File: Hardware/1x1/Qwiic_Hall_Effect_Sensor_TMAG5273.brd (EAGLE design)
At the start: 25.4 x 25.4 mm, 52 parts, among them J1 QWIIC_RIGHT_ANGLE, J2 QWIIC_RIGHT_ANGLE, Q1 20V/4.2A/52mΩ/1.4W, U1 TMAG5273

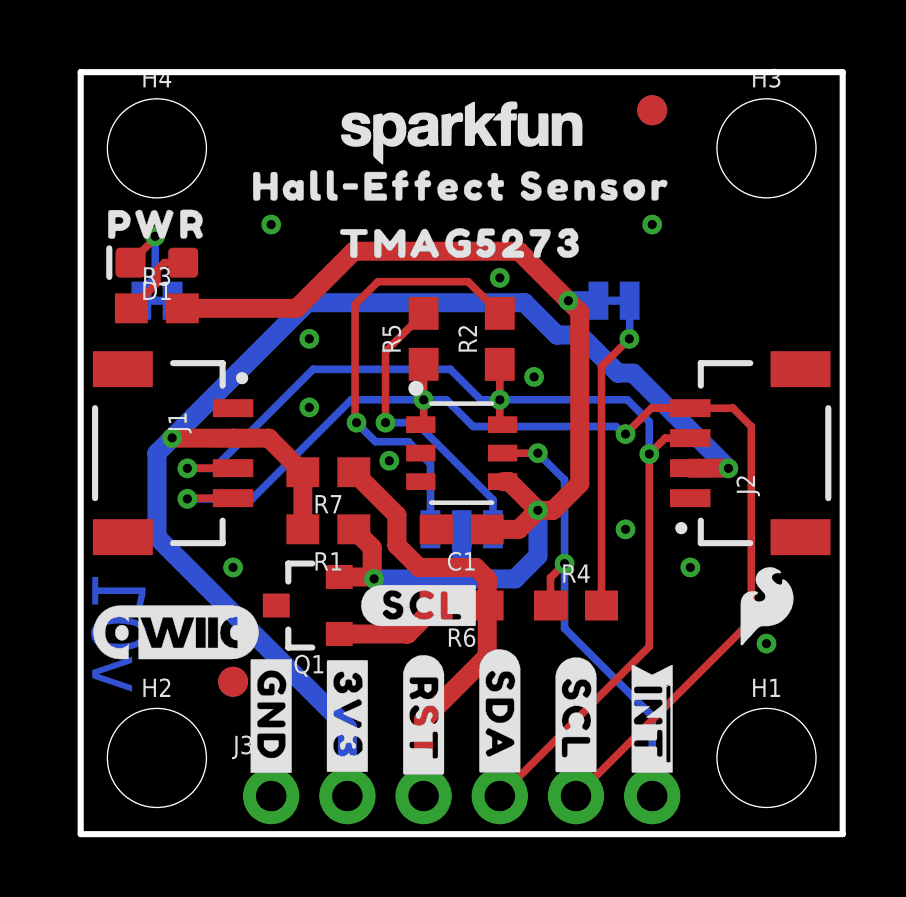
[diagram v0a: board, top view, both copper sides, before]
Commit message: Updates for design review
Changed LED and associated resistor to have the correct part and value; added dimension lines and further notes on the layout; adjusted aesthetics in schematic to now be the same as each other (minus the change in Qwiic connectors and number of standoffs)
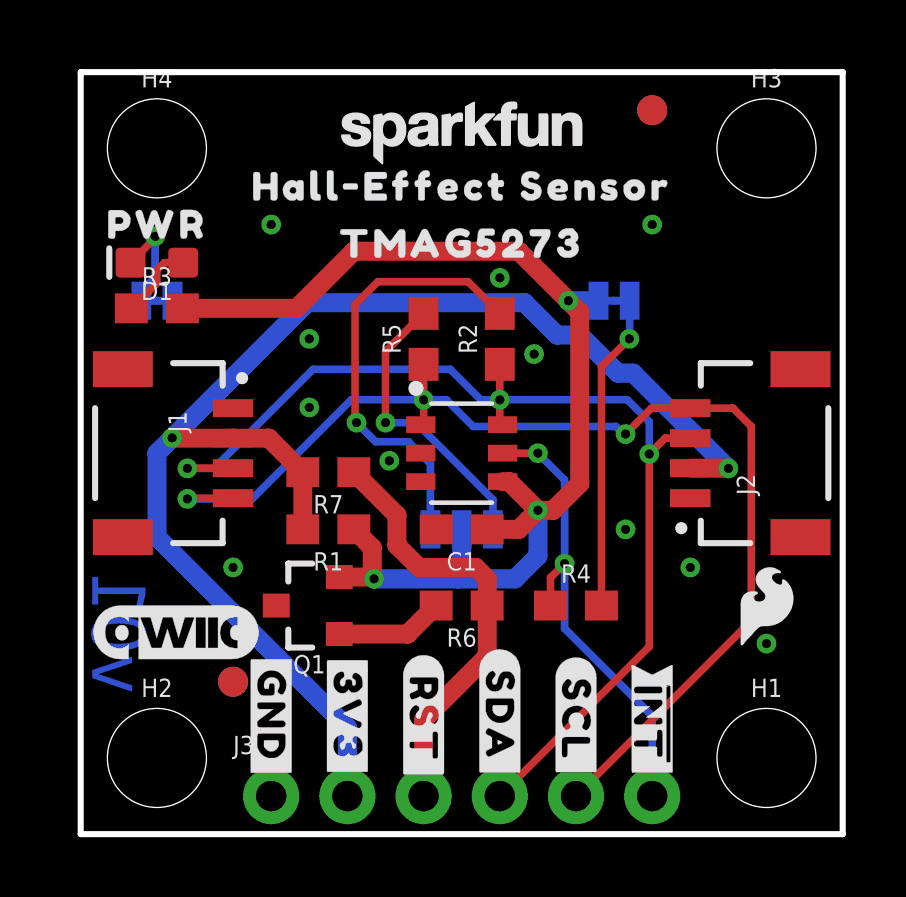
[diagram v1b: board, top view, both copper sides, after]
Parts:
- removed U$15: (no value), output:#SCL#5281
- D1: value RED -> Red
- R3: value 1k -> 4.7k
- moved FRAME1 16.6 mm to (-6.35, -40.6)
- moved LOGO5 16.5 mm to (44.5, 50.8)
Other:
- board text added: "Solder Mask: Red Thickness: 1.6mm Two layer design Finish: HASL Lead-Free Copper Weight: 1oz Material: TG135-140"
- board text added: "Units in inches"

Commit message: Ready for review
Updates from ENG Checklist - Small tweaks added  - updated ordering of PTH headers for SDA and SCL, fixed final errors on design
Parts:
- moved U$13 5.08 mm to (16.5, 4.70)
- moved U$5 5.08 mm to (16.5, 3.81)
- moved U$14 2.54 mm to (11.4, 3.94)
- moved U$16 2.54 mm to (14.0, 3.81)
- moved U$3 2.54 mm to (11.4, 3.94)
- moved U$4 2.54 mm to (14.0, 3.81)
- turned U$18 to 270 degrees
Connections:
- net GPIO: now also J3.5; no longer J3.3
- net SCL: now also J3.4; no longer J3.5
- net SDA: now also J3.3; no longer J3.4
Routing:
- net SCL: track 39.6 -> 42.1 mm
- net SDA: track 37.2 -> 39.7 mm
- net GPIO: track 14.6 -> 15.0 mm, vias 0 -> 1
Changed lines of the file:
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@@
 <layer number="37" name="tTest" color="7" fill="1" visible="no" active="yes"/>
 <layer number="38" name="bTest" color="7" fill="1" visible="no" active="yes"/>
-<layer number="39" name="tKeepout" color="4" fill="11" visible="yes" active="yes"/>
-<layer number="40" name="bKeepout" color="1" fill="11" visible="yes" active="yes"/>
-<layer number="41" name="tRestrict" color="4" fill="10" visible="yes" active="yes"/>
-<layer number="42" name="bRestrict" color="1" fill="10" visible="yes" active="yes"/>
+<layer number="39" name="tKeepout" color="4" fill="11" visible="no" active="yes"/>
+<layer number="40" name="bKeepout" color="1" fill="11" visible="no" active="yes"/>
+<layer number="41" name="tRestrict" color="4" fill="10" visible="no" active="yes"/>
+<layer number="42" name="bRestrict" color="1" fill="10" visible="no" active="yes"/>
 <layer number="43" name="vRestrict" color="2" fill="10" visible="no" active="yes"/>
 <layer number="44" name="Drills" color="7" fill="1" visible="no" active="yes"/>
@@
 <element name="U$2" library="output" package="#GND#36" value="" x="6.35" y="3.937" smashed="yes" rot="R270"/>
 <element name="U$1" library="output" package="#3V3#37" value="" x="8.89" y="3.937" smashed="yes" rot="R270"/>
-<element name="U$3" library="output" package="#SDA#37" value="" x="13.97" y="3.937" smashed="yes" rot="R270"/>
-<element name="U$4" library="output" package="#SCL#38" value="" x="16.51" y="3.81" smashed="yes" rot="R270"/>
+<element name="U$3" library="output" package="#SDA#37" value="" x="11.43" y="3.937" smashed="yes" rot="R270"/>
+<element name="U$4" library="output" package="#SCL#38" value="" x="13.97" y="3.81" smashed="yes" rot="R270"/>
 <element name="U$6" library="output" package="##INT#40" value="" x="19.05" y="3.683" smashed="yes" rot="R270"/>
 <element name="U$7" library="output" package="PWR41" value="" x="2.54" y="20.32" smashed="yes"/>
@@
 <attribute name="VALUE" x="7.62" y="9.271" size="0.6096" layer="27" font="vector" ratio="20" rot="R180" align="top-center"/>
 </element>
-<element name="U$13" library="output" package="#RESET#5278" value="" x="11.43" y="4.699" smashed="yes" rot="MR270"/>
-<element name="U$5" library="output" package="#RST#5279" value="" x="11.43" y="3.81" smashed="yes" rot="R270"/>
-<element name="U$14" library="output" package="#SDA#5280" value="" x="13.97" y="3.937" smashed="yes" rot="MR270"/>
-<element name="U$16" library="output" package="#SCL#5281" value="" x="16.51" y="3.81" smashed="yes" rot="MR270"/>
+<element name="U$13" library="output" package="#RESET#5278" value="" x="16.51" y="4.699" smashed="yes" rot="MR270"/>
+<element name="U$5" library="output" package="#RST#5279" value="" x="16.51" y="3.81" smashed="yes" rot="R270"/>
+<element name="U$14" library="output" package="#SDA#5280" value="" x="11.43" y="3.937" smashed="yes" rot="MR270"/>
+<element name="U$16" library="output" package="#SCL#5281" value="" x="13.97" y="3.81" smashed="yes" rot="MR270"/>
 <element name="U$17" library="output" package="##INT#5282" value="" x="19.05" y="3.683" smashed="yes" rot="MR270"/>
-<element name="U$18" library="output" package="#3V3#0" value="" x="8.89" y="3.937" smashed="yes" rot="MR90"/>
+<element name="U$18" library="output" package="#3V3#0" value="" x="8.89" y="3.937" smashed="yes" rot="MR270"/>
 <element name="U$19" library="output" package="#GND#4" value="" x="6.35" y="3.937" smashed="yes" rot="MR270"/>
 <element name="U$20" library="output" package="TMAG5273_HALL#EFFECT_SENSOR5" value="" x="12.065" y="15.24" smashed="yes" rot="MR0"/>
@@
 <contactref element="J1" pad="4"/>
 <contactref element="J2" pad="4"/>
-<contactref element="J3" pad="5"/>
 <wire x1="11.43" y1="14.478" x2="11.43" y2="13.74525" width="0.254" layer="1"/>
 <wire x1="11.43" y1="13.74525" x2="11.33475" y2="13.65" width="0.254" layer="1"/>
@@
 <wire x1="18.161" y1="13.335" x2="19.026" y2="14.2" width="0.254" layer="1"/>
 <wire x1="19.026" y1="14.2" x2="20.32" y2="14.2" width="0.254" layer="1"/>
-<wire x1="16.51" y1="1.27" x2="22.352" y2="7.112" width="0.254" layer="1"/>
 <wire x1="22.352" y1="7.112" x2="22.352" y2="13.589" width="0.254" layer="1"/>
 <wire x1="21.741" y1="14.2" x2="20.32" y2="14.2" width="0.254" layer="1"/>
 <wire x1="22.352" y1="13.589" x2="21.741" y2="14.2" width="0.254" layer="1"/>
+<contactref element="J3" pad="4"/>
+<wire x1="13.97" y1="1.27" x2="16.637" y2="3.937" width="0.254" layer="1"/>
+<wire x1="19.177" y1="3.937" x2="22.352" y2="7.112" width="0.254" layer="1"/>
+<wire x1="16.637" y1="3.937" x2="19.177" y2="3.937" width="0.254" layer="1"/>
 </signal>
 <signal name="SDA">
@@
 <contactref element="J1" pad="3"/>
 <contactref element="J2" pad="3"/>
-<contactref element="J3" pad="4"/>
 <wire x1="14.06525" y1="13.65" x2="13.97" y2="13.74525" width="0.254" layer="1"/>
 <wire x1="13.97" y1="13.74525" x2="13.97" y2="14.478" width="0.254" layer="1"/>
@@
 <wire x1="18.952540625" y1="12.670459375" x2="19.48208125" y2="13.2" width="0.254" layer="1"/>
 <wire x1="19.48208125" y1="13.2" x2="20.32" y2="13.2" width="0.254" layer="1"/>
-<wire x1="18.952540625" y1="12.670459375" x2="18.952540625" y2="6.252540625" width="0.254" layer="1"/>
-<wire x1="18.952540625" y1="6.252540625" x2="13.97" y2="1.27" width="0.254" layer="1"/>
+<wire x1="18.952540625" y1="12.670459375" x2="18.952540625" y2="6.35" width="0.254" layer="1"/>
+<contactref element="J3" pad="3"/>
+<wire x1="18.952540625" y1="6.35" x2="17.682540625" y2="5.08" width="0.254" layer="1"/>
+<wire x1="15.24" y1="5.08" x2="11.43" y2="1.27" width="0.254" layer="1"/>
+<wire x1="17.682540625" y1="5.08" x2="15.24" y2="5.08" width="0.254" layer="1"/>
 </signal>
 <signal name="N$4">
@@
 <signal name="GPIO">
 <contactref element="R6" pad="1"/>
-<contactref element="J3" pad="3"/>
 <contactref element="R7" pad="1"/>
 <wire x1="9.105" y1="12.065" x2="10.541" y2="10.629" width="0.635" layer="1"/>
@@
 <wire x1="10.541" y1="10.629" x2="10.541" y2="9.6274625" width="0.635" layer="1"/>
 <wire x1="11.2784625" y1="8.89" x2="13.169" y2="8.89" width="0.635" layer="1"/>
-<wire x1="11.43" y1="1.27" x2="11.43" y2="3.81" width="0.635" layer="1"/>
-<wire x1="13.55" y1="5.93" x2="13.55" y2="7.62" width="0.635" layer="1"/>
-<wire x1="11.43" y1="3.81" x2="13.55" y2="5.93" width="0.635" layer="1"/>
+<contactref element="J3" pad="5"/>
+<wire x1="13.55" y1="7.62" x2="13.55" y2="6.389" width="0.635" layer="1"/>
+<wire x1="13.55" y1="6.389" x2="13.589" y2="6.35" width="0.635" layer="1"/>
+<via x="13.589" y="6.35" extent="1-16" drill="0.381"/>
+<wire x1="13.589" y1="6.35" x2="16.51" y2="3.429" width="0.635" layer="16"/>
+<wire x1="16.51" y1="3.429" x2="16.51" y2="1.27" width="0.635" layer="16"/>
 </signal>
 <signal name="3.3V_SW">
@@
 </signals>
 <mfgpreviewcolors>
-<mfgpreviewcolor name="soldermaskcolor" color="0xC8FF0000"/>
+<mfgpreviewcolor name="soldermaskcolor" color="0xC8000000"/>
 <mfgpreviewcolor name="silkscreencolor" color="0xFFFEFEFE"/>
 <mfgpreviewcolor name="backgroundcolor" color="0xFF282828"/>

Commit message: Updated !INT silk
Updated !INT silk  to be the correct end (now ( rather than < )
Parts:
- removed U$17: (no value), output:##INT#5282
- added U$15: (no value), output:##INT#5276
- U$6: device output:##INT#40 -> output:##INT#5276
- flipped U$6 to the bottom
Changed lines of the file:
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@@
 <drawing>
 <settings>
-<setting alwaysvectorfont="yes"/>
+<setting alwaysvectorfont="no"/>
 <setting verticaltext="up"/>
 </settings>
@@
 <layer number="45" name="Holes" color="7" fill="1" visible="yes" active="yes"/>
 <layer number="46" name="Milling" color="3" fill="1" visible="no" active="yes"/>
-<layer number="47" name="Measures" color="7" fill="1" visible="yes" active="yes"/>
+<layer number="47" name="Measures" color="7" fill="1" visible="no" active="yes"/>
 <layer number="48" name="Document" color="7" fill="1" visible="no" active="yes"/>
 <layer number="49" name="Reference" color="7" fill="1" visible="no" active="yes"/>
@@
 <element name="U$3" library="output" package="#SDA#37" value="" x="11.43" y="3.937" smashed="yes" rot="R270"/>
 <element name="U$4" library="output" package="#SCL#38" value="" x="13.97" y="3.81" smashed="yes" rot="R270"/>
-<element name="U$6" library="output" package="##INT#40" value="" x="19.05" y="3.683" smashed="yes" rot="R270"/>
 <element name="U$7" library="output" package="PWR41" value="" x="2.54" y="20.32" smashed="yes"/>
 <element name="U$8" library="output" package="#LED#42" value="" x="5.461" y="17.78" smashed="yes" rot="MR0"/>
@@
 <element name="U$14" library="output" package="#SDA#5280" value="" x="11.43" y="3.937" smashed="yes" rot="MR270"/>
 <element name="U$16" library="output" package="#SCL#5281" value="" x="13.97" y="3.81" smashed="yes" rot="MR270"/>
-<element name="U$17" library="output" package="##INT#5282" value="" x="19.05" y="3.683" smashed="yes" rot="MR270"/>
 <element name="U$18" library="output" package="#3V3#0" value="" x="8.89" y="3.937" smashed="yes" rot="MR270"/>
 <element name="U$19" library="output" package="#GND#4" value="" x="6.35" y="3.937" smashed="yes" rot="MR270"/>
@@
 <attribute name="VALUE" x="2.54" y="16.764" size="0.6096" layer="27" font="vector" ratio="20" align="top-center"/>
 </element>
+<element name="U$15" library="output" package="##INT#5276" value="" x="19.05" y="3.683" smashed="yes" rot="R270"/>
+<element name="U$6" library="output" package="##INT#5276" value="" x="19.05" y="3.683" smashed="yes" rot="MR270"/>
 </elements>
 <signals>

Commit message: Design Review Changes
Adjusted schematic to have the correct power-on reset circuit, along with the change in the layout. The GPIO net was relabled to RESET to match the layout of the board/labeling. Adjusted some labeling in the schematic.
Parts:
- removed R1: 330, SparkFun-Resistors:0603
- removed R6: 10k, SparkFun-Resistors:0603
- moved R7 6.29 mm to (12.7, 7.62), turned to 0 degrees
- moved Q1 1.80 mm to (8.89, 8.89), turned to 180 degrees
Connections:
- net INT renamed !INT
- removed net GPIO: J3.5, R6.1, R7.1
- removed net N$7: Q1.1, R6.2
- new net RESET: J3.5, Q1.1, R7.2
- net 3.3V: now also Q1.2; no longer R1.2, R7.2
- net 3.3V_SW: now also Q1.3; no longer Q1.2, R1.1
- net GND: now also R7.1; no longer Q1.3
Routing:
- net GPIO: track 15.0 -> 0.00 mm, vias 1 -> 0
- net RESET: track 0.00 -> 14.1 mm, vias 0 -> 1
- net N$7: track 3.62 -> 0.00 mm
- net 3.3V_SW: track 38.9 -> 39.7 mm

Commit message: Adjusted from design review
Added truth tables, changed RESET to Disable, adjusted magnetic axis to be centered to the middle of the board, added push button for 1x1 reset option
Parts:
- added S1: (no value), SparkFun-Switches:TACTILE_SWITCH_SMD_4.6X2.8MM
- added U$17: (no value), output:#DISABLE#5280
- LOGO3: value QWIIC_LOGO_CONNECTOR -> QWIIC_LOGO_4MM; device SparkFun-Aesthetics:QWIIC_5.5MM -> SparkFun-Aesthetics:QWIIC_4MM
- U$13: device output:#RESET#5278 -> output:DISABLE5281
- U$5: device output:#RST#5279 -> output:#DISABLE#5280
- moved U$13 10.1 mm to (7.75, 9.78), flipped to the top, turned to 0 degrees
- moved Q1 3.74 mm to (8.26, 12.6)
- moved R4 3.42 mm to (17.8, 10.8), turned to 90 degrees
- moved U$5 1.65 mm to (16.5, 5.46), flipped to the bottom
- moved LOGO3 0.74 mm to (2.54, 6.35)
- moved R2 0.63 mm to (14.0, 17.1)
- moved R5 0.63 mm to (11.4, 17.1)
- moved U1 0.38 mm to (12.9, 13.0)
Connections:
- removed net RESET: J3.5, Q1.1, R7.2
- new net DISABLE: J3.5, Q1.1, R7.2, S1.1, S1.2
- net 3.3V: now also S1.3, S1.4
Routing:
- net DISABLE: track 0.00 -> 23.1 mm, vias 0 -> 1
- net RESET: track 14.1 -> 0.00 mm, vias 1 -> 0
- net 3.3V: track 46.0 -> 52.8 mm
- net N$5: track 10.5 -> 6.67 mm
- net SDA: track 39.7 -> 41.2 mm
- net SCL: track 42.1 -> 43.5 mm

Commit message: Design review updates
Addition of gerber files for both mini and 1x1, adjusted board for reds engineering checklist run.
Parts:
- moved Q1 2.67 mm to (8.26, 15.2)
- moved R7 1.42 mm to (14.0, 8.26)
- moved S1 1.42 mm to (8.89, 8.26)
- moved U$13 1.31 mm to (8.89, 10.4)
- moved C1 1.27 mm to (14.0, 10.2)
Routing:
- net 3.3V: track 52.8 -> 59.4 mm
- net SCL: track 43.5 -> 47.2 mm
- net DISABLE: track 23.1 -> 26.7 mm
- net SDA: track 41.2 -> 44.3 mm
- net 3.3V_SW: track 40.2 -> 43.3 mm
- net N$5: track 6.67 -> 7.73 mm
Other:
- board text added: "v10"
- board text removed: "v01"

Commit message: Updates from design review
Adjusted traces for better GND connections; changed direction of tail end for the DISABLE pin; changed jumper names in schematic to match layout; added more GND vias to the Mini; updated trace widths to be the correct size
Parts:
- U$15: device output:##INT#5276 -> output:#DISABLE#5290
- U$17, U$5: device output:#DISABLE#5280 -> output:#INT#5285
- U$6: device output:##INT#5276 -> output:#INT#5289
- U$9: device output:##INT#43 -> output:#DISABLE#5290
- moved U$6 14.2 mm to (20.6, 17.8), turned to 0 degrees
- moved U$9 12.9 mm to (16.5, 5.59), flipped to the top, turned to 270 degrees
- moved U$15 3.17 mm to (16.5, 5.59), flipped to the bottom
- moved U$17 3.10 mm to (19.1, 3.68), flipped to the bottom
- moved U$5 3.10 mm to (19.1, 3.68), flipped to the top
- moved FD3 1.27 mm to (20.3, 24.1)
- moved FD4 1.27 mm to (20.3, 24.1)
- renumbered JP1 to I2C, JP3 to LED
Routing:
- net 3.3V_SW: track 43.3 -> 40.8 mm
- net N$5: track 7.73 -> 9.70 mm
- net !INT: track 16.2 -> 15.5 mm
- net 3.3V: track 59.4 -> 58.8 mm
